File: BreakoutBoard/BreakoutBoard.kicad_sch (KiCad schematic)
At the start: 7 parts, among them J1 addon_conn, J2 Power, J3 Power, J4 Conn_01x09, J5 Conn_01x10

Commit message: Fixes directory for BreakoutBoard
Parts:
- H1, H2: footprint (none) -> MountingHole:MountingHole_2.2mm_M2_Pad_Via
- J2, J3: footprint (none) -> Connector_PinHeader_2.54mm:PinHeader_2x02_P2.54mm_Vertical
- J4: footprint (none) -> Connector_PinHeader_2.54mm:PinHeader_1x09_P2.54mm_Vertical
- J5: footprint (none) -> Connector_PinHeader_2.54mm:PinHeader_1x10_P2.54mm_Vertical
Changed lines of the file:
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@@
       (effects (font (size 1.27 1.27)))
     )
-    (property "Footprint" "" (id 2) (at 113.03 146.05 0)
+    (property "Footprint" "Connector_PinHeader_2.54mm:PinHeader_2x02_P2.54mm_Vertical" (id 2) (at 113.03 146.05 0)
       (effects (font (size 1.27 1.27)) hide)
     )
@@
       (effects (font (size 1.27 1.27)) (justify left))
     )
-    (property "Footprint" "" (id 2) (at 222.25 91.44 0)
+    (property "Footprint" "MountingHole:MountingHole_2.2mm_M2_Pad_Via" (id 2) (at 222.25 91.44 0)
       (effects (font (size 1.27 1.27)) hide)
     )
@@
       (effects (font (size 1.27 1.27)))
     )
-    (property "Footprint" "" (id 2) (at 148.59 146.05 0)
+    (property "Footprint" "Connector_PinHeader_2.54mm:PinHeader_2x02_P2.54mm_Vertical" (id 2) (at 148.59 146.05 0)
       (effects (font (size 1.27 1.27)) hide)
     )
@@
       (effects (font (size 1.27 1.27)) (justify left))
     )
-    (property "Footprint" "" (id 2) (at 209.55 91.44 0)
+    (property "Footprint" "MountingHole:MountingHole_2.2mm_M2_Pad_Via" (id 2) (at 209.55 91.44 0)
       (effects (font (size 1.27 1.27)) hide)
     )
@@
       (effects (font (size 1.27 1.27)) (justify left))
     )
-    (property "Footprint" "" (id 2) (at 160.02 63.5 0)
+    (property "Footprint" "Connector_PinHeader_2.54mm:PinHeader_1x09_P2.54mm_Vertical" (id 2) (at 160.02 63.5 0)
       (effects (font (size 1.27 1.27)) hide)
     )
@@
       (effects (font (size 1.27 1.27)) (justify left))
     )
-    (property "Footprint" "" (id 2) (at 160.02 101.6 0)
-      (effects (font (size 1.27 1.27)) hide)
-    )
+    (property "Footprint" "Connector_PinHeader_2.54mm:PinHeader_1x10_P2.54mm_Vertical" (id 2) (at 160.02 101.6 0)
+      (effects (font (size 1.27 1.27)) hide)
+    )

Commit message: Uses different conn_02x02 symbol that matches footprint
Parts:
- removed J2, J3: Power, Connector_PinHeader_2.54mm:PinHeader_2x02_P2.54mm_Vertical, symbol Connector_Generic:Conn_02x02_Row_Letter_Last
- added J2, J3: (no value), symbol Connector_Generic:Conn_02x02_Odd_Even
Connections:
- net +3V3: now also J2.1 (Pin_1), J2.2 (Pin_2), J3.1 (Pin_1), J3.2 (Pin_2)
- net GND: now also J2.3 (Pin_3), J2.4 (Pin_4), J3.3 (Pin_3), J3.4 (Pin_4)

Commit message: Removes mouting holes from breakout board
This will be on a breadboard. It doesn't need mouting holes
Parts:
- removed H1, H2: ~, MountingHole:MountingHole_2.2mm_M2_Pad_Via, symbol Mechanical:MountingHole_Pad
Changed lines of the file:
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@@
   (junction (at 105.41 54.61) (diameter 0) (color 0 0 0 0)
   )
-  (junction (at 215.9 97.79) (diameter 0) (color 0 0 0 0)
-  )
   (wire (pts (xy 143.51 99.06) (xy 143.51 86.36))
     (stroke (width 0) (type default))
@@
     (stroke (width 0) (type default))
   )
-  (wire (pts (xy 215.9 97.79) (xy 222.25 97.79))
-    (stroke (width 0) (type default))
-  )
   (wire (pts (xy 105.41 52.07) (xy 105.41 54.61))
     (stroke (width 0) (type default))
@@
     (stroke (width 0) (type default))
   )
-  (wire (pts (xy 209.55 93.98) (xy 209.55 97.79))
-    (stroke (width 0) (type default))
-  )
-  (wire (pts (xy 209.55 97.79) (xy 215.9 97.79))
-    (stroke (width 0) (type default))
-  )
   (wire (pts (xy 105.41 151.13) (xy 105.41 148.59))
     (stroke (width 0) (type default))
@@
   )
   (wire (pts (xy 130.81 111.76) (xy 154.94 111.76))
-    (stroke (width 0) (type default))
-  )
-  (wire (pts (xy 222.25 97.79) (xy 222.25 93.98))
     (stroke (width 0) (type default))
   )
@@
     (pin "4")
   )
-  (symbol (lib_id "Mechanical:MountingHole_Pad") (at 222.25 91.44 0) (unit 1)
-    (in_bom yes) (on_board yes) (fields_autoplaced)
-    (property "Reference" "H2" (id 0) (at 224.79 89.535 0)
-      (effects (font (size 1.27 1.27)) (justify left))
-    )
-    (property "Value" "~" (id 1) (at 224.79 91.44 0)
-      (effects (font (size 1.27 1.27)) (justify left))
-    )
-    (property "Footprint" "MountingHole:MountingHole_2.2mm_M2_Pad_Via" (id 2) (at 222.25 91.44 0)
-      (effects (font (size 1.27 1.27)) hide)
-    )
-    (property "Datasheet" "~" (id 3) (at 222.25 91.44 0)
-      (effects (font (size 1.27 1.27)) hide)
-    )
-    (pin "1")
-  )
   (symbol (lib_id "power:PWR_FLAG") (at 105.41 107.95 90) (unit 1)
     (in_bom yes) (on_board yes) (fields_autoplaced)
@@
     )
     (property "Datasheet" "" (id 3) (at 152.4 76.2 0)
-      (effects (font (size 1.27 1.27)) hide)
-    )
-    (pin "1")
-  )
-  (symbol (lib_id "power:GND") (at 215.9 97.79 0) (unit 1)
-    (in_bom yes) (on_board yes) (fields_autoplaced)
-    (property "Reference" "#PWR015" (id 0) (at 215.9 104.14 0)
-      (effects (font (size 1.27 1.27)) hide)
-    )
-    (property "Value" "GND" (id 1) (at 215.9 102.87 0)
-      (effects (font (size 1.27 1.27)))
-    )
-    (property "Footprint" "" (id 2) (at 215.9 97.79 0)
-      (effects (font (size 1.27 1.27)) hide)
-    )
-    (property "Datasheet" "" (id 3) (at 215.9 97.79 0)
       (effects (font (size 1.27 1.27)) hide)
     )
@@
     (pin "1")
   )
-  (symbol (lib_id "Mechanical:MountingHole_Pad") (at 209.55 91.44 0) (unit 1)
-    (in_bom yes) (on_board yes) (fields_autoplaced)
-    (property "Reference" "H1" (id 0) (at 212.09 89.535 0)
-      (effects (font (size 1.27 1.27)) (justify left))
-    )
-    (property "Value" "~" (id 1) (at 212.09 91.44 0)
-      (effects (font (size 1.27 1.27)) (justify left))
-    )
-    (property "Footprint" "MountingHole:MountingHole_2.2mm_M2_Pad_Via" (id 2) (at 209.55 91.44 0)
-      (effects (font (size 1.27 1.27)) hide)
-    )
-    (property "Datasheet" "~" (id 3) (at 209.55 91.44 0)
-      (effects (font (size 1.27 1.27)) hide)
-    )
-    (pin "1")
-  )
   (symbol (lib_id "Connector_Generic:Conn_01x09") (at 160.02 63.5 0) (unit 1)
     (in_bom yes) (on_board yes) (fields_autoplaced)
@@
       (reference "#PWR014") (unit 1) (value "GND") (footprint "")
     )
-    (path "/42c4b14d-4b6d-4d53-8eab-1aff6020c8e2"
-      (reference "#PWR015") (unit 1) (value "GND") (footprint "")
-    )
-    (path "/9c8dd6e5-227d-42fe-b0d8-979d4f25aaa2"
-      (reference "H1") (unit 1) (value "~") (footprint "MountingHole:MountingHole_2.2mm_M2_Pad_Via")
-    )
-    (path "/239f5f69-032f-46f0-9d61-ca8a943cc10a"
-      (reference "H2") (unit 1) (value "~") (footprint "MountingHole:MountingHole_2.2mm_M2_Pad_Via")
-    )
     (path "/53c4401f-d4b1-47e2-aa52-ad488e1ad521"

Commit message: Adds revision number to PCBs
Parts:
- J2: value (none) -> Power_top; footprint (none) -> Connector_PinHeader_2.54mm:PinHeader_2x02_P2.54mm_Vertical
- J3: value (none) -> Power_bottom; footprint (none) -> Connector_PinHeader_2.54mm:PinHeader_2x02_P2.54mm_Vertical
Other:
- title: (none) -> GameOver breakout board
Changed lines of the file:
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@@
 (kicad_sch (version 20220331) (generator eeschema)
   (paper "A4")
+  (title_block
+    (title "GameOver breakout board")
+    (rev "0.1")
+  )
   (junction (at 105.41 107.95) (diameter 0) (color 0 0 0 0)
   )
@@
       (effects (font (size 1.27 1.27)))
     )
-    (property "Value" "" (id 1) (at 149.86 152.4 0)
-      (effects (font (size 1.27 1.27)))
-    )
-    (property "Footprint" "" (id 2) (at 148.59 146.05 0)
+    (property "Value" "Power_bottom" (id 1) (at 149.86 152.4 0)
+      (effects (font (size 1.27 1.27)))
+    )
+    (property "Footprint" "Connector_PinHeader_2.54mm:PinHeader_2x02_P2.54mm_Vertical" (id 2) (at 148.59 146.05 0)
       (effects (font (size 1.27 1.27)) hide)
     )
@@
       (effects (font (size 1.27 1.27)))
     )
-    (property "Value" "" (id 1) (at 115.57 152.4 0)
-      (effects (font (size 1.27 1.27)))
-    )
-    (property "Footprint" "" (id 2) (at 113.03 146.05 0)
-      (effects (font (size 1.27 1.27)) hide)
-    )
+    (property "Value" "Power_top" (id 1) (at 115.57 152.4 0)
+      (effects (font (size 1.27 1.27)))
+    )
+    (property "Footprint" "Connector_PinHeader_2.54mm:PinHeader_2x02_P2.54mm_Vertical" (id 2) (at 113.03 146.05 0)
+      (effects (font (size 1.27 1.27)) hide)
+    )

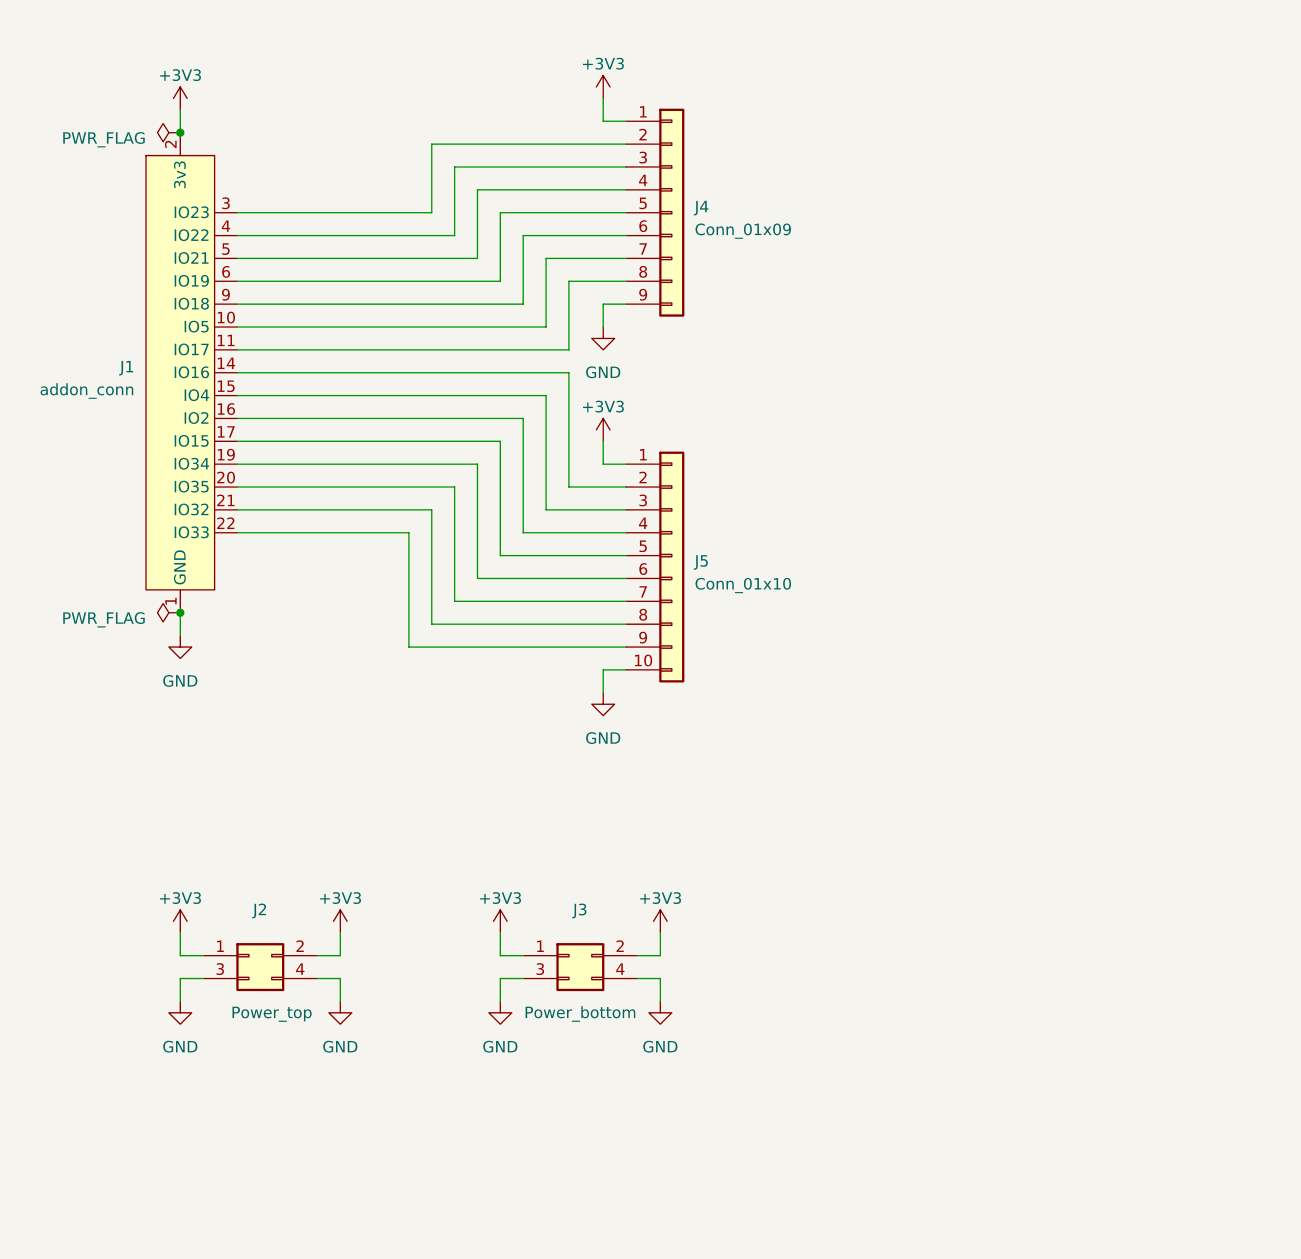
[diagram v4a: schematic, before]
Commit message: Adapts breakout board to changes in the addon connector
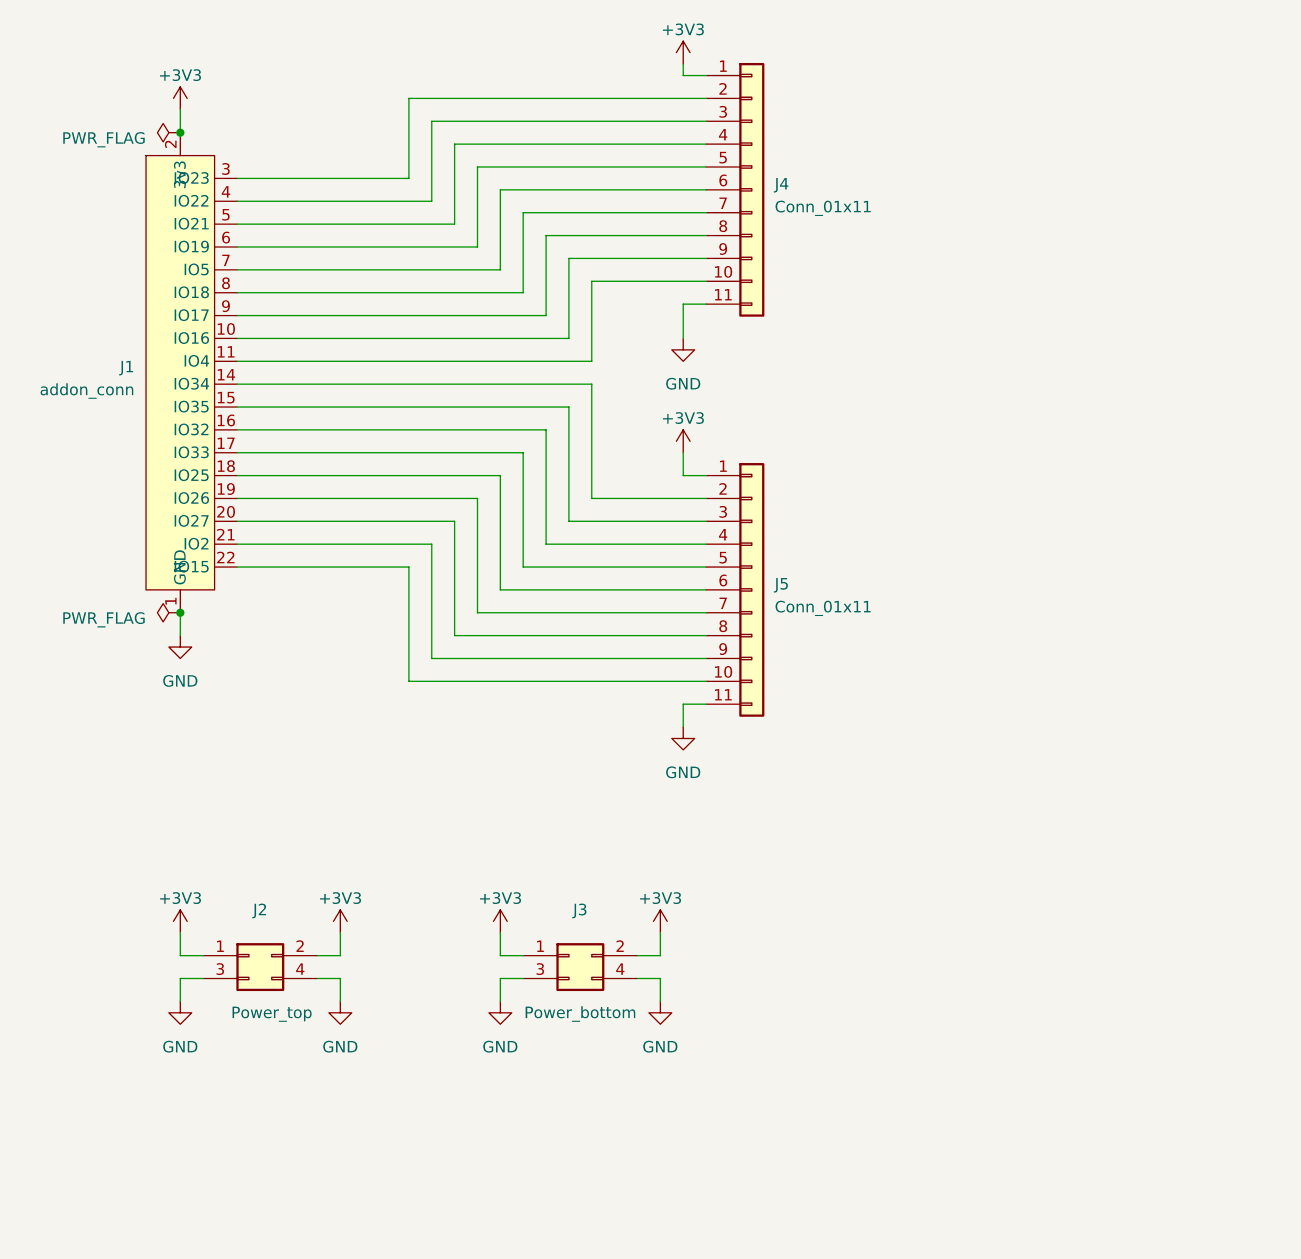
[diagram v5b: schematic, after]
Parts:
- removed J4: Conn_01x09, Connector_PinHeader_2.54mm:PinHeader_1x09_P2.54mm_Vertical, symbol Connector_Generic:Conn_01x09
- removed J5: Conn_01x10, Connector_PinHeader_2.54mm:PinHeader_1x10_P2.54mm_Vertical, symbol Connector_Generic:Conn_01x10
- added J4, J5: Conn_01x11, Connector_PinHeader_2.54mm:PinHeader_1x11_P2.54mm_Vertical, symbol Connector_Generic:Conn_01x11
- J1: footprint GameOver:TXGA_FFC05036-24SBD113W5M_1x24_P0.50mm_Horizontal -> GameOver:Addon_conn_TXGA_FFC05036-24SBD113W5M_1x24_P0.50mm_Horizontal
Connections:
- net +3V3: now also J4.1 (Pin_1), J5.1 (Pin_1); no longer J1.8 (3v3)
- net GND: now also J4.11 (Pin_11), J5.11 (Pin_11); no longer J1.18 (GND), J1.7 (GND)
- net at J1.10 (IO16): now also J4.9 (Pin_9)
- net at J1.11 (IO4): now also J4.10 (Pin_10)
- net at J1.14 (IO34): now also J5.2 (Pin_2)
- net at J1.15 (IO35): now also J5.3 (Pin_3)
- net at J1.16 (IO32): now also J5.4 (Pin_4)
- net at J1.17 (IO33): now also J5.5 (Pin_5)
- net at J1.19 (IO26): now also J5.7 (Pin_7)
- net at J1.20 (IO27): now also J5.8 (Pin_8)
- net at J1.21 (IO2): now also J5.9 (Pin_9)
- net at J1.22 (IO15): now also J5.10 (Pin_10)
- net at J1.3 (IO23): now also J4.2 (Pin_2)
- net at J1.4 (IO22): now also J4.3 (Pin_3)
- net at J1.5 (IO21): now also J4.4 (Pin_4)
- net at J1.6 (IO19): now also J4.5 (Pin_5)
- net at J1.9 (IO17): now also J4.8 (Pin_8)
- new net: J1.18 (IO25), J5.6 (Pin_6)
- new net: J1.7 (IO5), J4.6 (Pin_6)
- new net: J1.8 (IO18), J4.7 (Pin_7)

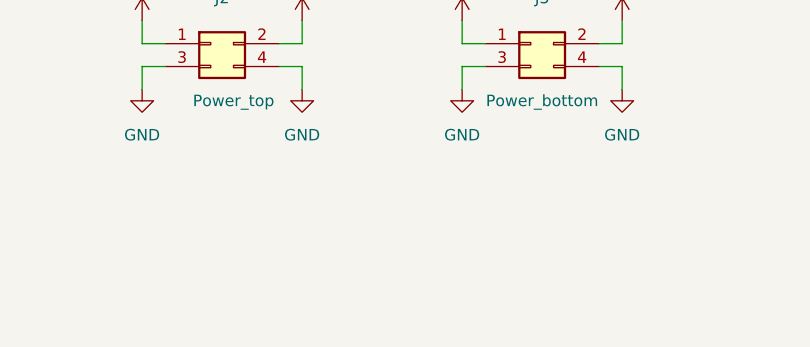
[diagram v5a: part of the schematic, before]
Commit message: Adds logo to breakout board schematics
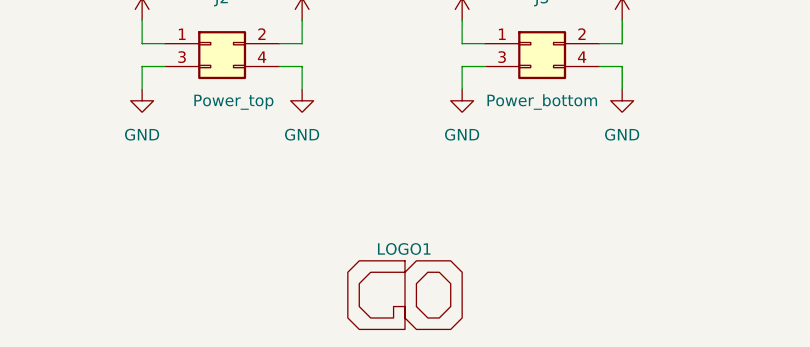
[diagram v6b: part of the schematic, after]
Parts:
- added LOGO1: GameOver_logo, symbol GameOver:GameOver_logo
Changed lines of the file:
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@@
     (pin "1")
+  )
+  (symbol (lib_id "GameOver:GameOver_logo") (at 134.62 173.99 0) (unit 1)
+    (in_bom no) (on_board yes)
+    (property "Reference" "LOGO1" (id 0) (at 131.445 168.91 0)
+      (effects (font (size 1.27 1.27)) (justify left))
+    )
+    (property "Value" "GameOver_logo" (id 1) (at 134.62 180.34 0)
+      (effects (font (size 1.27 1.27)) hide)
+    )
+    (property "Footprint" "" (id 2) (at 134.62 173.99 0)
+      (effects (font (size 1.27 1.27)) hide)
+    )
+    (property "Datasheet" "" (id 3) (at 134.62 173.99 0)
+      (effects (font (size 1.27 1.27)) hide)
+    )
   )
   (symbol (lib_id "power:GND") (at 161.29 77.47 0) (unit 1)
@@
       (reference "J5") (unit 1) (value "Conn_01x11") (footprint "Connector_PinHeader_2.54mm:PinHeader_1x11_P2.54mm_Vertical")
     )
-  )
+    (path "/362c7b82-6a16-4785-b44b-851dfe11b1ab"
+      (reference "LOGO1") (unit 1) (value "GameOver_logo") (footprint "GameOver:logo_fcu")
+    )
+  )

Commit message: Updates logo in the BreakoutBoard
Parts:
- LOGO1: footprint (none) -> GameOver:logo_fcu
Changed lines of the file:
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@@
       (effects (font (size 1.27 1.27)) hide)
     )
-    (property "Footprint" "" (id 2) (at 134.62 173.99 0)
+    (property "Footprint" "GameOver:logo_fcu" (id 2) (at 134.62 173.99 0)
       (effects (font (size 1.27 1.27)) hide)
     )

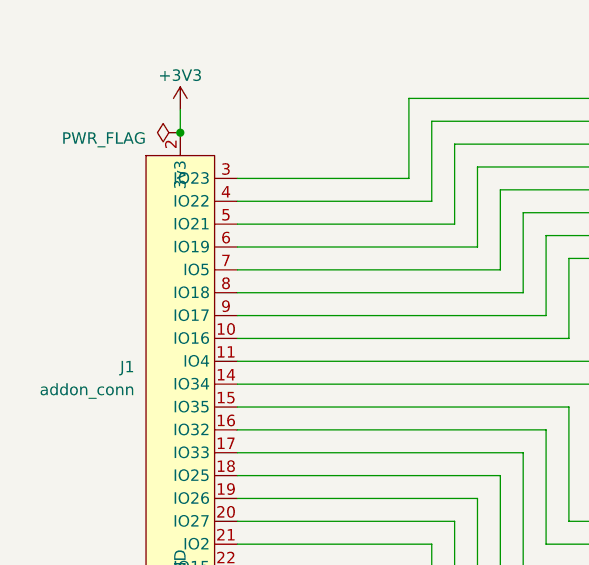
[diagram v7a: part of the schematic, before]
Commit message: Updates all add-on boards with fix introduced in 692041
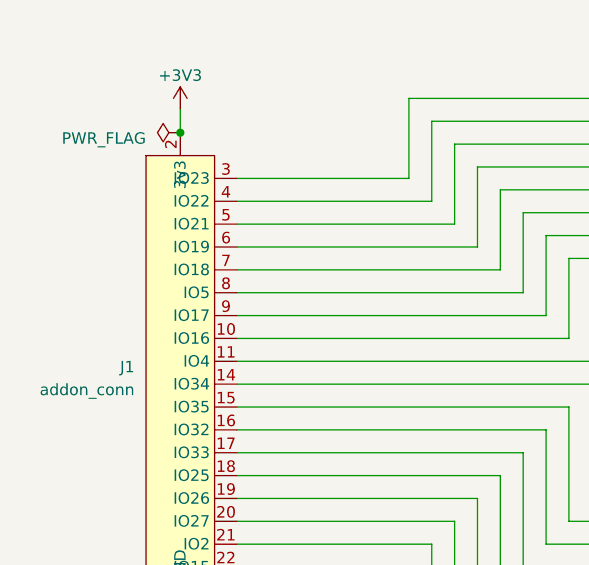
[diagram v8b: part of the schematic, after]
